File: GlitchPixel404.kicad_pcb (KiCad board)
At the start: 2 copper layers, 50 x 34 mm, 35 parts, among them J1 USB_C_Receptacle_USB2.0_16P, J2 VOLTLINK, J5 Barrel_Jack_Switch, J7 Output, Q1 AONR21357-ES, Q2 MMBT3904, SW1 Reset, U1 ESP32-PICO-MINI-02U-N8R2, U2 SN74LVC2T45DCUR, U3 CH224K, U4 CH340N, U5 SN74LVC2T45DCUR, U7 MCP1792x-5002xCB

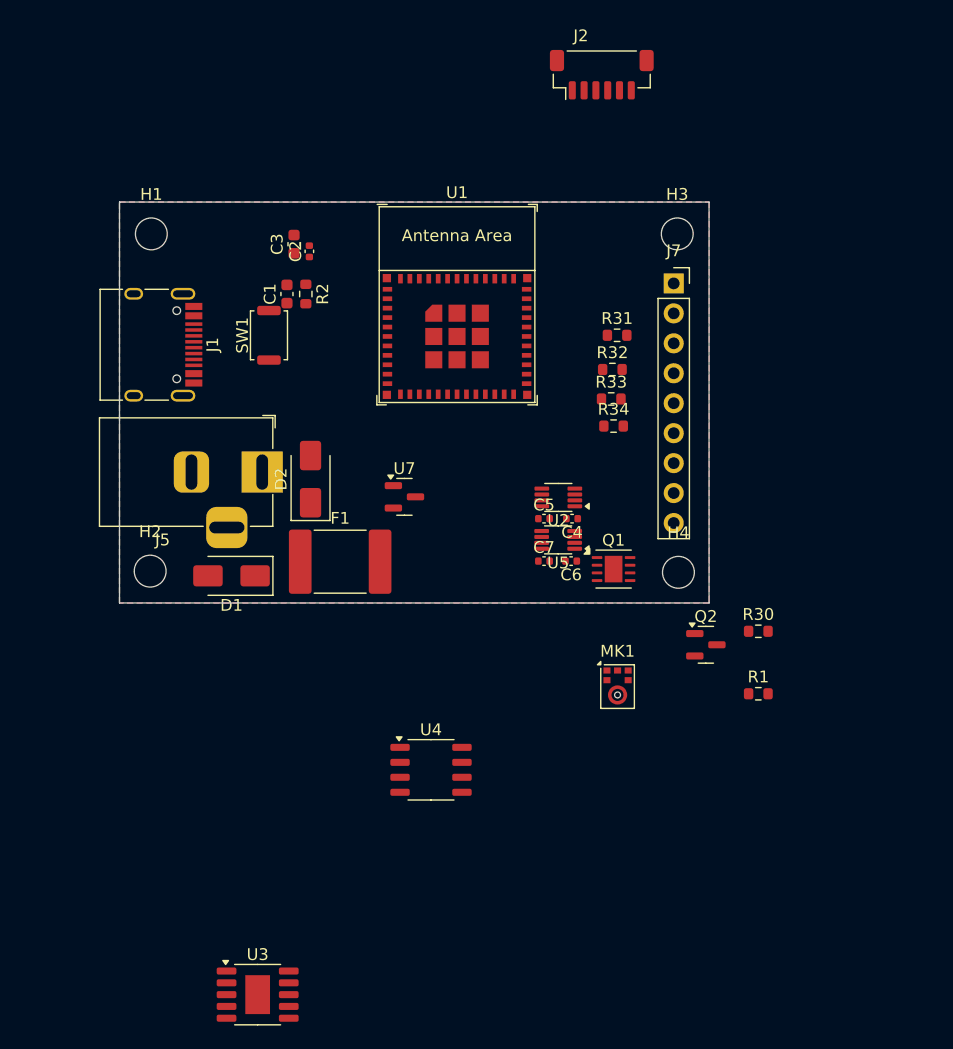
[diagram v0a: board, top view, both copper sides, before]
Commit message: Add USB PD Trig Circuit
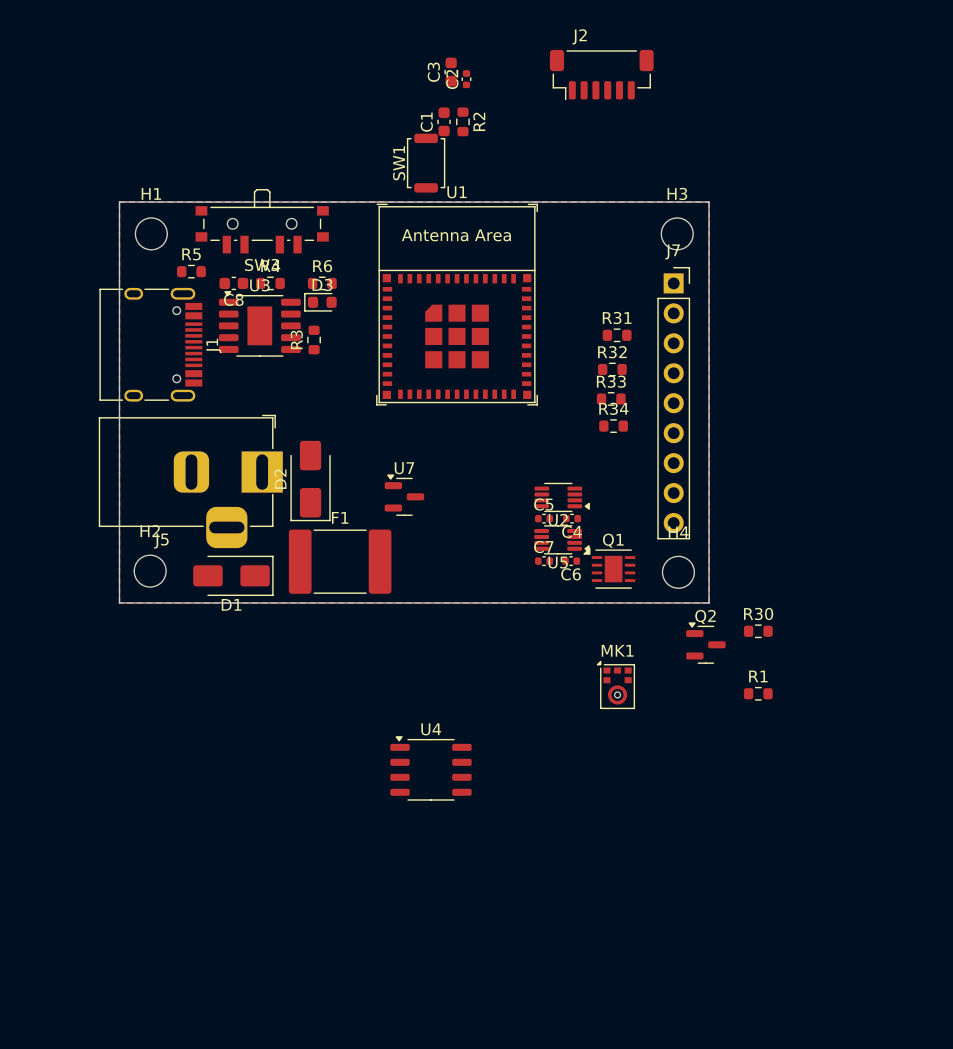
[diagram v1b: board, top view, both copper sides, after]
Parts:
- added C8: 1uF, Capacitor_SMD:C_0603_1608Metric, F.Cu at (109.7, 72.9)
- added D3: LED_Small, LED_SMD:LED_0603_1608Metric, F.Cu at (117.2, 74.5)
- added R3: 10k, Resistor_SMD:R_0603_1608Metric, F.Cu at (116.5, 77.7)
- added R4: 1k, Resistor_SMD:R_0603_1608Metric, F.Cu at (112.8, 72.9)
- added R5: 24k, Resistor_SMD:R_0603_1608Metric, F.Cu at (106.1, 71.9)
- added R6: 10k, Resistor_SMD:R_0603_1608Metric, F.Cu at (117.2, 72.9)
- added SW3: SW_SP3T, Button_Switch_SMD:SW_SP3T_PCM13, F.Cu at (112.1, 68.2)
- moved U3 56.7 mm to (111.9, 76.5)
- moved C2 19.8 mm to (129.4, 55.6)
- moved C3 19.8 mm to (128.1, 55.0)
- moved C1 19.8 mm to (127.5, 59.2)
- moved R2 19.8 mm to (129.1, 59.2)
- moved SW1 19.8 mm to (126.0, 62.7)
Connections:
- net Net-(J1-VBUS-PadA4) renamed VBUS
- J1 pad A1: Net-(J1-GND-PadA1) -> GND
- J1 pad A12: Net-(J1-GND-PadA1) -> GND
- J1 pad A5: unconnected-(J1-CC1-PadA5) -> Net-(J1-CC1)
- J1 pad A6: unconnected-(J1-D+-PadA6) -> Net-(U3-DP)
- J1 pad A7: unconnected-(J1-D--PadA7) -> Net-(U3-DM)
- J1 pad B1: Net-(J1-GND-PadA1) -> GND
- J1 pad B12: Net-(J1-GND-PadA1) -> GND
- J1 pad B5: unconnected-(J1-CC2-PadB5) -> Net-(J1-CC2)
- J1 pad B6: unconnected-(J1-D+-PadB6) -> Net-(U3-DP)
- J1 pad B7: unconnected-(J1-D--PadB7) -> Net-(U3-DM)
- J1 pad S1: unconnected-(J1-SHIELD-PadS1) -> GND
- U3 pad 1: unconnected-(U3-VDD-Pad1) -> VDD
- U3 pad 10: unconnected-(U3-PG-Pad10) -> PG
- U3 pad 11: unconnected-(U3-GND-Pad11) -> GND
- U3 pad 4: unconnected-(U3-DP-Pad4) -> Net-(U3-DP)
- U3 pad 5: unconnected-(U3-DM-Pad5) -> Net-(U3-DM)
- U3 pad 6: unconnected-(U3-CC2-Pad6) -> Net-(J1-CC2)
- U3 pad 7: unconnected-(U3-CC1-Pad7) -> Net-(J1-CC1)
- U3 pad 8: unconnected-(U3-VBUS-Pad8) -> Net-(U3-VBUS)
- U3 pad 9: unconnected-(U3-CFG1-Pad9) -> Net-(U3-CFG1)

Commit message: Changed buffers to 74LVC2G34 and added datasheets
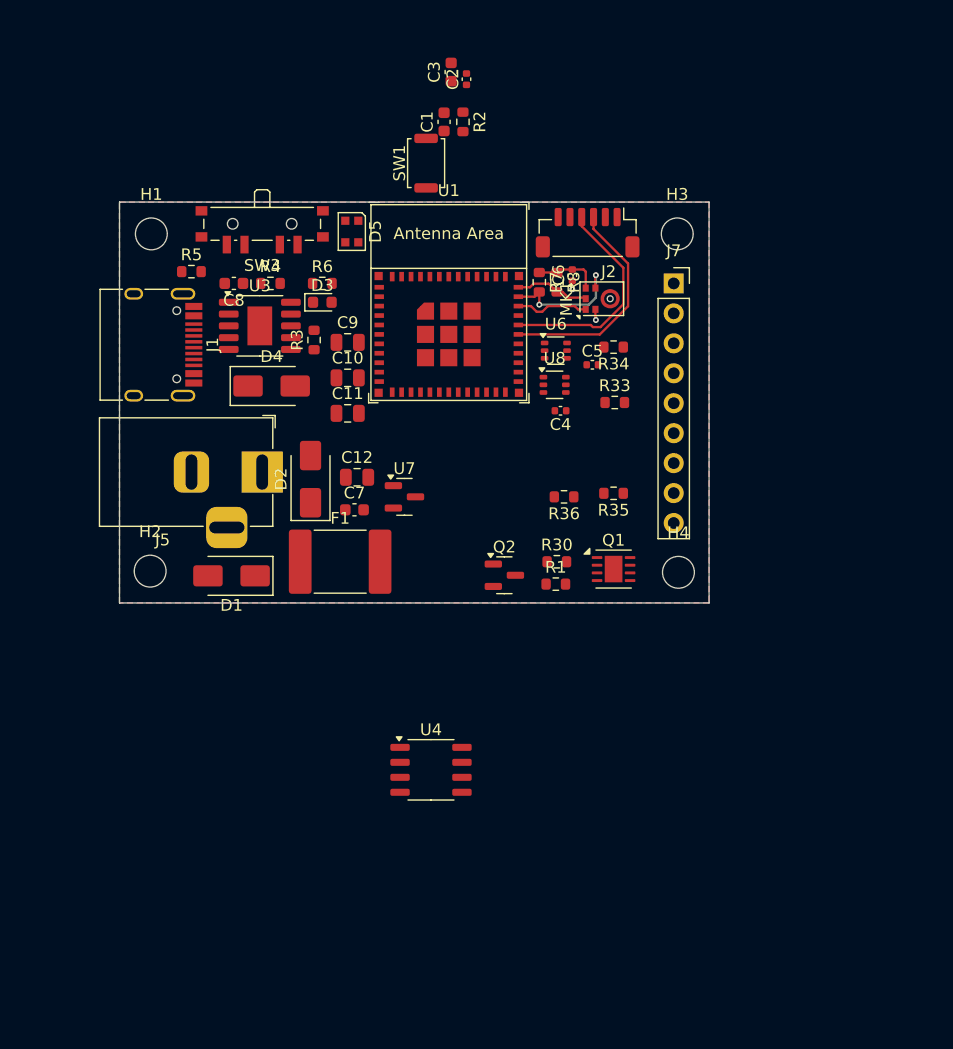
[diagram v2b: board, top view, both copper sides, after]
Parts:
- removed R31, R32: 100R, Resistor_SMD:R_0603_1608Metric
- removed U2, U5: SN74LVC2T45DCUR, Package_SO:VSSOP-8_2.3x2mm_P0.5mm
- added C10: 22uF/25V, Capacitor_SMD:C_0805_2012Metric, F.Cu at (119.3, 80.9)
- added C11: 22uF/25V, Capacitor_SMD:C_0805_2012Metric, F.Cu at (119.3, 83.9)
- added C12: 22uF/25V, Capacitor_SMD:C_0805_2012Metric, F.Cu at (120.1, 89.3)
- added C9: 22uF/25V, Capacitor_SMD:C_0805_2012Metric, F.Cu at (119.3, 77.9)
- added D4: SMAJ24A, Diode_SMD:D_SMA, F.Cu at (112.9, 81.6)
- added D5: WS2812B-2020, LED_SMD:LED_WS2812B-2020_PLCC4_2.0x2.0mm, F.Cu at (119.7, 68.5)
- added R35: 100R, Resistor_SMD:R_0603_1608Metric, F.Cu at (141.9, 90.7)
- added R36: 100R, Resistor_SMD:R_0603_1608Metric, F.Cu at (137.7, 91.0)
- added R7: 10k, Resistor_SMD:R_0603_1608Metric, F.Cu at (135.6, 72.8)
- added R8: 10k, Resistor_SMD:R_0603_1608Metric, F.Cu at (137.1, 72.8)
- added U6: 74LVC2G34, Package_TO_SOT_SMD:SOT-363_SC-70-6, F.Cu at (137.0, 78.6)
- added U8: 74LVC2G34, Package_TO_SOT_SMD:SOT-363_SC-70-6, F.Cu at (136.9, 81.5)
- C3: value 22uF -> 22uF/6.3V
- C7: value 100nF -> 22uF/6.3V; footprint Capacitor_SMD:C_0402_1005Metric -> Capacitor_SMD:C_0603_1608Metric
- U7: value MCP1792x-5002xCB -> HE2021A50HMR
- moved MK1 32.9 mm to (140.9, 74.2), turned to 90 degrees
- moved C6 24.3 mm to (138.4, 72.2), turned to 90 degrees
- moved R1 19.5 mm to (137.0, 98.4)
- moved R30 18.1 mm to (137.1, 96.5)
- moved Q2 18.1 mm to (132.6, 97.7)
- moved C7 16.7 mm to (119.9, 92.1)
- moved C5 13.7 mm to (140.1, 79.8)
- moved J2 13.5 mm to (139.7, 68.6), turned to 180 degrees
- moved C4 9.20 mm to (137.4, 83.7)
- moved R34 6.70 mm to (141.9, 78.3), turned to 180 degrees
- moved U1 0.72 mm to (127.9, 77.2)
- moved R33 0.42 mm to (142.0, 83.0)
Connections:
- net Net-(D1-A) renamed /VDC
- C5 pad 1: +3.3V -> +5V
- C6 pad 1: +5V -> GND
- C6 pad 2: GND -> +3.3V
- C7 pad 1: +3.3V -> +5V
- D2 pad 2: unconnected-(D2-A-Pad2) -> VBUS
- MK1 pad 1: unconnected-(MK1-WS-Pad1) -> MIC_WS
- MK1 pad 2: unconnected-(MK1-LR-Pad2) -> GND
- MK1 pad 3: unconnected-(MK1-GND-Pad3) -> GND
- MK1 pad 4: unconnected-(MK1-SCK-Pad4) -> SCL
- MK1 pad 5: unconnected-(MK1-VDD-Pad5) -> +3.3V
- MK1 pad 6: unconnected-(MK1-SD-Pad6) -> SDA
- U1 pad 26: unconnected-(U1-GPIO20-Pad26) -> S4
- U1 pad 27: unconnected-(U1-SD_DATA_0/GPIO7-Pad27) -> S3
- U1 pad 28: unconnected-(U1-SD_DATA_1/GPIO8-Pad28) -> S2
- U1 pad 29: unconnected-(U1-GPIO5-Pad29) -> S1
- U1 pad 33: unconnected-(U1-GPIO19-Pad33) -> MIC_WS
- U1 pad 34: unconnected-(U1-GPIO22-Pad34) -> SCL
- U1 pad 35: unconnected-(U1-GPIO21-Pad35) -> SDA
- U1 pad 4: unconnected-(U1-SENSOR_VP/GPIO36/ADC1_CH0-Pad4) -> Net-(D5-DIN)
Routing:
- net /RXD: track 0.00 -> 19.1 mm
- net /TXD: track 0.00 -> 18.6 mm
- net SCL: track 0.00 -> 11.1 mm, vias 0 -> 2
- net SDA: track 0.00 -> 6.36 mm
- net MIC_WS: track 0.00 -> 6.33 mm
- net +3.3V: track 0.06 -> 5.57 mm
- net GND: track 0.00 -> 1.64 mm, vias 0 -> 2

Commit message: Added 3v3 DCDC
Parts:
- added C13: 100nF, Capacitor_SMD:C_0402_1005Metric, F.Cu at (118.7, 102.5)
- added C14: 56pF, Capacitor_SMD:C_0402_1005Metric, F.Cu at (118.7, 104.5)
- added C15: 22uF/6.3V, Capacitor_SMD:C_0603_1608Metric, F.Cu at (114.1, 107.4)
- added C16: 22uF/6.3V, Capacitor_SMD:C_0603_1608Metric, F.Cu at (114.1, 109.9)
- added R10: 22.1K, Resistor_SMD:R_0402_1005Metric, F.Cu at (117.6, 109.1)
- added R9: 100K, Resistor_SMD:R_0402_1005Metric, F.Cu at (117.6, 107.1)
- added U2: TPS54202DDC, Package_TO_SOT_SMD:SOT-23-6, F.Cu at (114.7, 103.9)

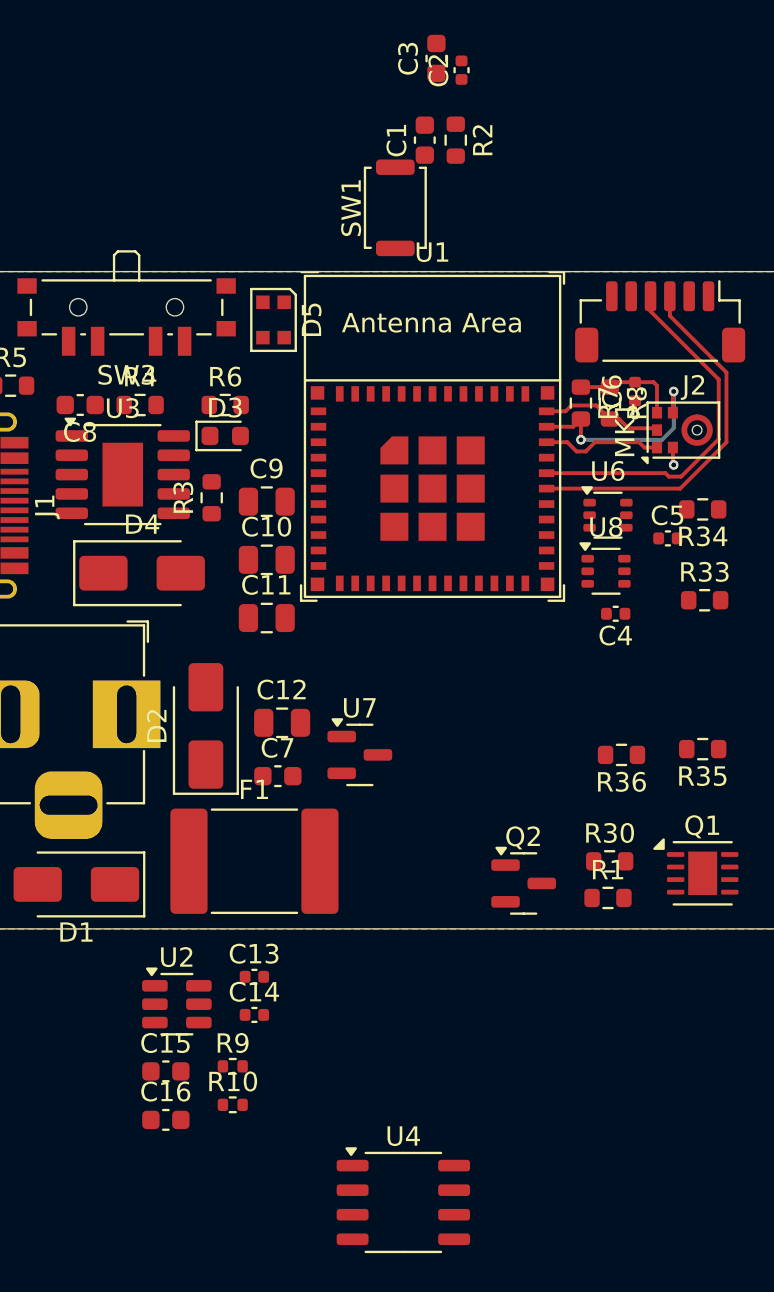
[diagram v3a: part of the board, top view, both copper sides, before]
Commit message: Parts selection and 0402
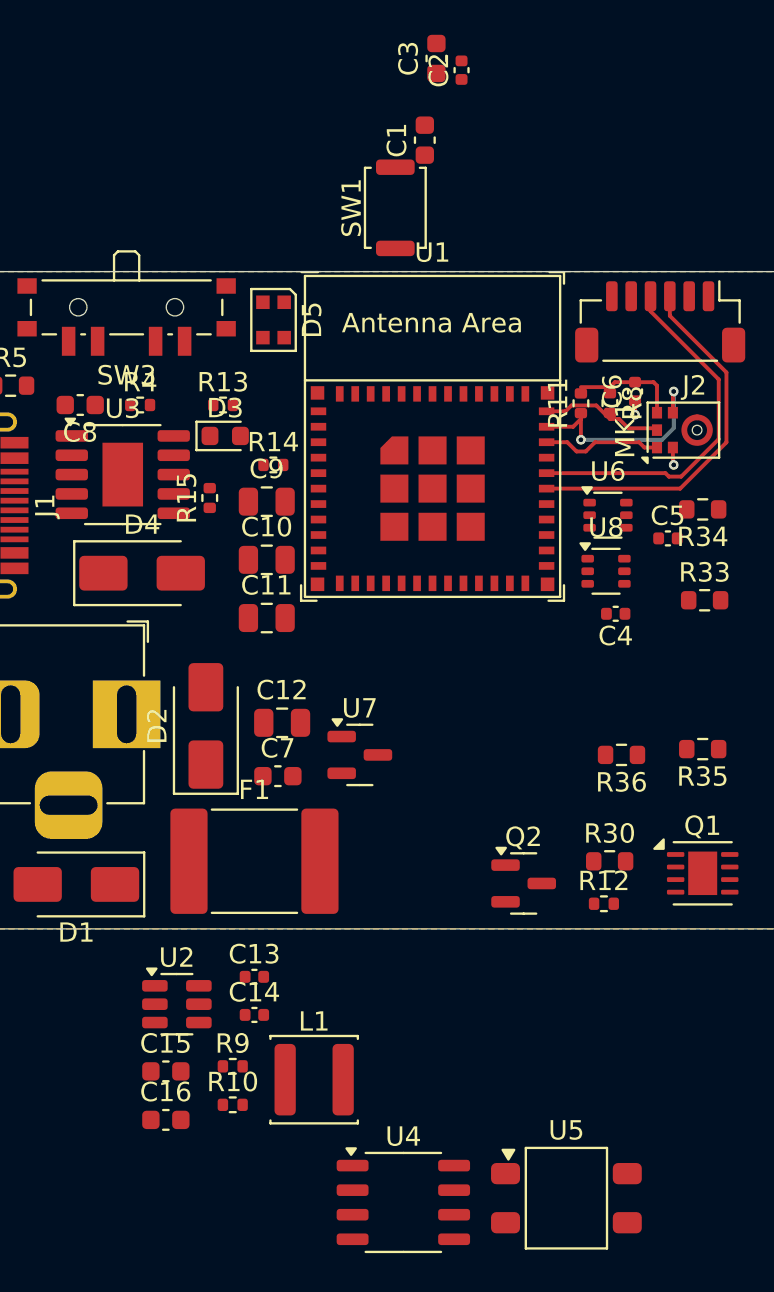
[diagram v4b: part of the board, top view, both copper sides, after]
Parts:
- removed R1: 100k, Resistor_SMD:R_0603_1608Metric
- removed R2, R3, R6, R7: 10k, Resistor_SMD:R_0603_1608Metric
- added L1: 10uH, Inductor_SMD:L_Changjiang_FNR4018S, F.Cu at (121.8, 107.8)
- added R11: 10k, Resistor_SMD:R_0402_1005Metric, F.Cu at (135.6, 72.8)
- added R12: 100K, Resistor_SMD:R_0402_1005Metric, F.Cu at (136.8, 98.7)
- added R13: 10k, Resistor_SMD:R_0402_1005Metric, F.Cu at (117.1, 72.9)
- added R14: 10k, Resistor_SMD:R_0402_1005Metric, F.Cu at (119.7, 76.0)
- added R15: 10k, Resistor_SMD:R_0402_1005Metric, F.Cu at (116.4, 77.7)
- added U5: IRM-H6xxT, OptoDevice:Everlight_IRM-H6xxT, F.Cu at (134.8, 113.9)
- C14: value 56pF -> 47pF
- R10: value 22.1K -> 22K
- R4, R8: footprint Resistor_SMD:R_0603_1608Metric -> Resistor_SMD:R_0402_1005Metric
